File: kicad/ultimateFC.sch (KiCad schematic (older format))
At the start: 195 parts, among them J1 USB_B_Micro, J2 10132797-011100LF, J3 10132797-011100LF, J4 10132797-011100LF, J5 10132797-011100LF, J6 10132797-011100LF, Q1 DMP2066LSN-7, U1 EFM8BB21F16G-C-QFN20R, U10 NCP81253MNTBG, U11 SiZ200DT, U12 NCP81253MNTBG, U13 SiZ200DT, U14 TPS62824ADMQ, U15 SiZ200DT, U16 NCP81253MNTBG, U17 NCP81253MNTBG, U18 NCP81253MNTBG, U19 NCP81253MNTBG, U2 EFM8BB21F16G-C-QFN20R, U20 SiZ200DT, U21 SiZ200DT, U22 SiZ200DT, U23 SiZ200DT, U24 EFM8BB21F16G-C-QFN20R, U25 NCP81253MNTBG, U26 SiZ200DT, U27 NCP81253MNTBG, U28 NCP81253MNTBG, U29 SiZ200DT, U3 NCP81253MNTBG, U30 SiZ200DT, U31 INA186, U32 LMR33630CQRNX, U33 STM32F745VGHx, U34 AB7456, U35 ZOE-M8Q_ZOE-M8Q, U36 ICM-20602, U37 S25FL064L, U39 BMP280, U4 SiZ200DT, U5 TPS630701, U6 EFM8BB21F16G-C-QFN20R, U7 NCP81253MNTBG, U8 SiZ200DT, U9 NCP81253MNTBG, X1 Molex_734120110, Y1 CSTNE8M00G550000R0, Y2 ECS-270-8-47Q-CES-TR

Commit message: swap ESC gate role names, add schematic pdf
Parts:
- J1: symbol Connector:USB_B_Micro -> ultimateFC-rescue:USB_B_Micro-Connector
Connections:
- net Ac_ESC_1: now also RN14.3 (R3.1), RN14.5 (R4.2), U1.14 (P1.0), U18.2 (PWM); no longer RN14.6 (R3.2), U1.13 (P1.1)
- net Ac_ESC_2: now also RN13.3 (R3.1), RN13.5 (R4.2), U2.14 (P1.0), U3.2 (PWM); no longer RN13.6 (R3.2), U2.13 (P1.1)
- net Ac_ESC_3: now also RN15.3 (R3.1), RN15.5 (R4.2), U19.2 (PWM), U6.14 (P1.0); no longer RN15.6 (R3.2), U6.13 (P1.1)
- net Ac_ESC_4: now also RN20.3 (R3.1), RN20.5 (R4.2), U24.14 (P1.0), U28.2 (PWM); no longer RN20.6 (R3.2), U24.13 (P1.1)
- net Ap_ESC_1: now also RN14.6 (R3.2), U1.13 (P1.1); no longer RN14.3 (R3.1), RN14.5 (R4.2), U1.14 (P1.0), U18.2 (PWM)
- net Ap_ESC_2: now also RN13.6 (R3.2), U2.13 (P1.1); no longer RN13.3 (R3.1), RN13.5 (R4.2), U2.14 (P1.0), U3.2 (PWM)
- net Ap_ESC_3: now also RN15.6 (R3.2), U6.13 (P1.1); no longer RN15.3 (R3.1), RN15.5 (R4.2), U19.2 (PWM), U6.14 (P1.0)
- net Ap_ESC_4: now also RN20.6 (R3.2), U24.13 (P1.1); no longer RN20.3 (R3.1), RN20.5 (R4.2), U24.14 (P1.0), U28.2 (PWM)
- net Bc_ESC_1: now also RN14.2 (R2.1), RN14.8 (R1.2), U1.10 (P1.3), U10.2 (PWM); no longer RN14.7 (R2.2), U1.11 (P1.2)
- net Bc_ESC_2: now also RN13.2 (R2.1), RN13.8 (R1.2), U2.10 (P1.3), U7.2 (PWM); no longer RN13.7 (R2.2), U2.11 (P1.2)
- net Bc_ESC_3: now also RN15.2 (R2.1), RN15.8 (R1.2), U12.2 (PWM), U6.10 (P1.3); no longer RN15.7 (R2.2), U6.11 (P1.2)
- net Bc_ESC_4: now also RN20.2 (R2.1), RN20.8 (R1.2), U24.10 (P1.3), U25.2 (PWM); no longer RN20.7 (R2.2), U24.11 (P1.2)
- net Bp_ESC_1: now also RN14.7 (R2.2), U1.11 (P1.2); no longer RN14.2 (R2.1), RN14.8 (R1.2), U1.10 (P1.3), U10.2 (PWM)
- net Bp_ESC_2: now also RN13.7 (R2.2), U2.11 (P1.2); no longer RN13.2 (R2.1), RN13.8 (R1.2), U2.10 (P1.3), U7.2 (PWM)
- net Bp_ESC_3: now also RN15.7 (R2.2), U6.11 (P1.2); no longer RN15.2 (R2.1), RN15.8 (R1.2), U12.2 (PWM), U6.10 (P1.3)
- net Bp_ESC_4: now also RN20.7 (R2.2), U24.11 (P1.2); no longer RN20.2 (R2.1), RN20.8 (R1.2), U24.10 (P1.3), U25.2 (PWM)
- net Cc_ESC_1: now also R16.2, R17.1, U1.9 (P1.4), U16.2 (PWM); no longer R17.2, U1.8 (P1.5)
- net Cc_ESC_2: now also R26.2, R27.1, U2.9 (P1.4), U9.2 (PWM); no longer R27.2, U2.8 (P1.5)
- net Cc_ESC_3: now also R18.2, R19.1, U17.2 (PWM), U6.9 (P1.4); no longer R19.2, U6.8 (P1.5)
- net Cc_ESC_4: now also R28.2, R29.1, U24.9 (P1.4), U27.2 (PWM); no longer R29.2, U24.8 (P1.5)
- net Cp_ESC_1: now also R17.2, U1.8 (P1.5); no longer R16.2, R17.1, U1.9 (P1.4), U16.2 (PWM)
- net Cp_ESC_2: now also R27.2, U2.8 (P1.5); no longer R26.2, R27.1, U2.9 (P1.4), U9.2 (PWM)
- net Cp_ESC_3: now also R19.2, U6.8 (P1.5); no longer R18.2, R19.1, U17.2 (PWM), U6.9 (P1.4)
- net Cp_ESC_4: now also R29.2, U24.8 (P1.5); no longer R28.2, R29.1, U24.9 (P1.4), U27.2 (PWM)
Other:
- note added: "public files:\nhttps://github.com/crteensy/Yolo-files"
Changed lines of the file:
@@
 EESchema Schematic File Version 4
-LIBS:ultimateFC-cache
 EELAYER 30 0
 EELAYER END
@@
 Sheet 1 1
 Title "ESCs and Power"
-Date "2020-05-26"
-Rev "0"
+Date "2021-04-22"
+Rev "1"
 Comp ""
 Comment1 ""
@@
 Text GLabel 11050 2325 0    50   Input ~ 0
 ESC_2_TX
-Text GLabel 12450 1825 2    50   Input ~ 0
-Ap_ESC_2
 Text GLabel 12450 1925 2    50   Input ~ 0
+Ap_ESC_2
+Text GLabel 12450 1825 2    50   Input ~ 0
 Ac_ESC_2
-Text GLabel 12450 2125 2    50   Input ~ 0
-Bp_ESC_2
 Text GLabel 12450 2025 2    50   Input ~ 0
+Bp_ESC_2
+Text GLabel 12450 2125 2    50   Input ~ 0
 Bc_ESC_2
-Text GLabel 12450 2225 2    50   Input ~ 0
-Cp_ESC_2
 Text GLabel 12450 2325 2    50   Input ~ 0
+Cp_ESC_2
+Text GLabel 12450 2225 2    50   Input ~ 0
 Cc_ESC_2
 NoConn ~ 12450 2425
@@
 NoConn ~ 11050 2525
 NoConn ~ 11050 2625
-Text GLabel 15650 1875 0    50   Input ~ 0
+Text GLabel 15650 1775 0    50   Input ~ 0
 Ac_ESC_2
-Text GLabel 15675 2075 0    50   Input ~ 0
+Text GLabel 15675 1975 0    50   Input ~ 0
 Bp_ESC_2
-Text GLabel 14700 4025 0    50   Input ~ 0
-Cp_ESC_2
 Text GLabel 14700 4125 0    50   Input ~ 0
+Cp_ESC_2
+Text GLabel 14700 4025 0    50   Input ~ 0
 Cc_ESC_2
 $Comp
@@
 Wire Wire Line
 	16800 4450 16950 4450
-Text GLabel 15650 1775 0    50   Input ~ 0
+Text GLabel 15650 1875 0    50   Input ~ 0
 Ap_ESC_2
 Wire Wire Line
@@
 Text GLabel 16125 2225 3    50   Input ~ 0
 LS_2_B
-Text GLabel 15675 1975 0    50   Input ~ 0
+Text GLabel 15675 2075 0    50   Input ~ 0
 Bc_ESC_2
 $Comp
@@
 Text GLabel 1775 2325 0    50   Input ~ 0
 ESC_1_TX
-Text GLabel 3175 1825 2    50   Input ~ 0
-Ap_ESC_1
 Text GLabel 3175 1925 2    50   Input ~ 0
+Ap_ESC_1
+Text GLabel 3175 1825 2    50   Input ~ 0
 Ac_ESC_1
-Text GLabel 3175 2125 2    50   Input ~ 0
-Bp_ESC_1
 Text GLabel 3175 2025 2    50   Input ~ 0
+Bp_ESC_1
+Text GLabel 3175 2125 2    50   Input ~ 0
 Bc_ESC_1
-Text GLabel 3175 2225 2    50   Input ~ 0
-Cp_ESC_1
 Text GLabel 3175 2325 2    50   Input ~ 0
+Cp_ESC_1
+Text GLabel 3175 2225 2    50   Input ~ 0
 Cc_ESC_1
 NoConn ~ 3175 2425
@@
 NoConn ~ 1775 2525
 NoConn ~ 1775 2625
-Text GLabel 6375 1875 0    50   Input ~ 0
+Text GLabel 6375 1775 0    50   Input ~ 0
 Ac_ESC_1
-Text GLabel 6400 2075 0    50   Input ~ 0
+Text GLabel 6400 1975 0    50   Input ~ 0
 Bp_ESC_1
-Text GLabel 5425 4025 0    50   Input ~ 0
-Cp_ESC_1
 Text GLabel 5425 4125 0    50   Input ~ 0
+Cp_ESC_1
+Text GLabel 5425 4025 0    50   Input ~ 0
 Cc_ESC_1
 $Comp
@@
 Wire Wire Line
 	7525 4450 7675 4450
-Text GLabel 6375 1775 0    50   Input ~ 0
+Text GLabel 6375 1875 0    50   Input ~ 0
 Ap_ESC_1
 Wire Wire Line
@@
 Text GLabel 6850 2225 3    50   Input ~ 0
 LS_1_B
-Text GLabel 6400 1975 0    50   Input ~ 0
+Text GLabel 6400 2075 0    50   Input ~ 0
 Bc_ESC_1
 Wire Wire Line
@@
 Text GLabel 1800 7275 0    50   Input ~ 0
 ESC_3_TX
-Text GLabel 3200 6775 2    50   Input ~ 0
-Ap_ESC_3
 Text GLabel 3200 6875 2    50   Input ~ 0
+Ap_ESC_3
+Text GLabel 3200 6775 2    50   Input ~ 0
 Ac_ESC_3
-Text GLabel 3200 7075 2    50   Input ~ 0
-Bp_ESC_3
 Text GLabel 3200 6975 2    50   Input ~ 0
+Bp_ESC_3
+Text GLabel 3200 7075 2    50   Input ~ 0
 Bc_ESC_3
-Text GLabel 3200 7175 2    50   Input ~ 0
-Cp_ESC_3
 Text GLabel 3200 7275 2    50   Input ~ 0
+Cp_ESC_3
+Text GLabel 3200 7175 2    50   Input ~ 0
 Cc_ESC_3
 NoConn ~ 3200 7375
@@
 NoConn ~ 1800 7475
 NoConn ~ 1800 7575
-Text GLabel 6400 6825 0    50   Input ~ 0
+Text GLabel 6400 6725 0    50   Input ~ 0
 Ac_ESC_3
-Text GLabel 6425 7025 0    50   Input ~ 0
+Text GLabel 6425 6925 0    50   Input ~ 0
 Bp_ESC_3
-Text GLabel 5450 8975 0    50   Input ~ 0
-Cp_ESC_3
 Text GLabel 5450 9075 0    50   Input ~ 0
+Cp_ESC_3
+Text GLabel 5450 8975 0    50   Input ~ 0
 Cc_ESC_3
 $Comp
@@
 Wire Wire Line
 	7550 9400 7700 9400
-Text GLabel 6400 6725 0    50   Input ~ 0
+Text GLabel 6400 6825 0    50   Input ~ 0
 Ap_ESC_3
 Wire Wire Line
@@
 Text GLabel 6875 7175 3    50   Input ~ 0
 LS_3_B
-Text GLabel 6425 6925 0    50   Input ~ 0
+Text GLabel 6425 7025 0    50   Input ~ 0
 Bc_ESC_3
 Wire Wire Line
@@
 Text GLabel 11050 7275 0    50   Input ~ 0
 ESC_4_TX
-Text GLabel 12450 6775 2    50   Input ~ 0
-Ap_ESC_4
 Text GLabel 12450 6875 2    50   Input ~ 0
+Ap_ESC_4
+Text GLabel 12450 6775 2    50   Input ~ 0
 Ac_ESC_4
-Text GLabel 12450 7075 2    50   Input ~ 0
-Bp_ESC_4
 Text GLabel 12450 6975 2    50   Input ~ 0
+Bp_ESC_4
+Text GLabel 12450 7075 2    50   Input ~ 0
 Bc_ESC_4
-Text GLabel 12450 7175 2    50   Input ~ 0
-Cp_ESC_4
 Text GLabel 12450 7275 2    50   Input ~ 0
+Cp_ESC_4
+Text GLabel 12450 7175 2    50   Input ~ 0
 Cc_ESC_4
 NoConn ~ 12450 7375
@@
 NoConn ~ 11050 7475
 NoConn ~ 11050 7575
-Text GLabel 15650 6825 0    50   Input ~ 0
+Text GLabel 15650 6725 0    50   Input ~ 0
 Ac_ESC_4
-Text GLabel 15675 7025 0    50   Input ~ 0
+Text GLabel 15675 6925 0    50   Input ~ 0
 Bp_ESC_4
-Text GLabel 14700 8975 0    50   Input ~ 0
-Cp_ESC_4
 Text GLabel 14700 9075 0    50   Input ~ 0
+Cp_ESC_4
+Text GLabel 14700 8975 0    50   Input ~ 0
 Cc_ESC_4
 $Comp
@@
 Wire Wire Line
 	16800 9400 16950 9400
-Text GLabel 15650 6725 0    50   Input ~ 0
+Text GLabel 15650 6825 0    50   Input ~ 0
 Ap_ESC_4
 Wire Wire Line
@@
 Text GLabel 16125 7175 3    50   Input ~ 0
 LS_4_B
-Text GLabel 15675 6925 0    50   Input ~ 0
+Text GLabel 15675 7025 0    50   Input ~ 0
 Bc_ESC_4
 Wire Wire Line
@@
 	25750 1175 25850 1175
 $Comp
-L Connector:USB_B_Micro J?
+L ultimateFC-rescue:USB_B_Micro-Connector J?
 U 1 1 5F57339B
 P 27000 2425
@@
 Wire Wire Line
 	10300 14775 10000 14775
+Text Notes 26325 10600 0    150  ~ 0
+public files:\nhttps://github.com/crteensy/Yolo-files
 $EndSCHEMATC

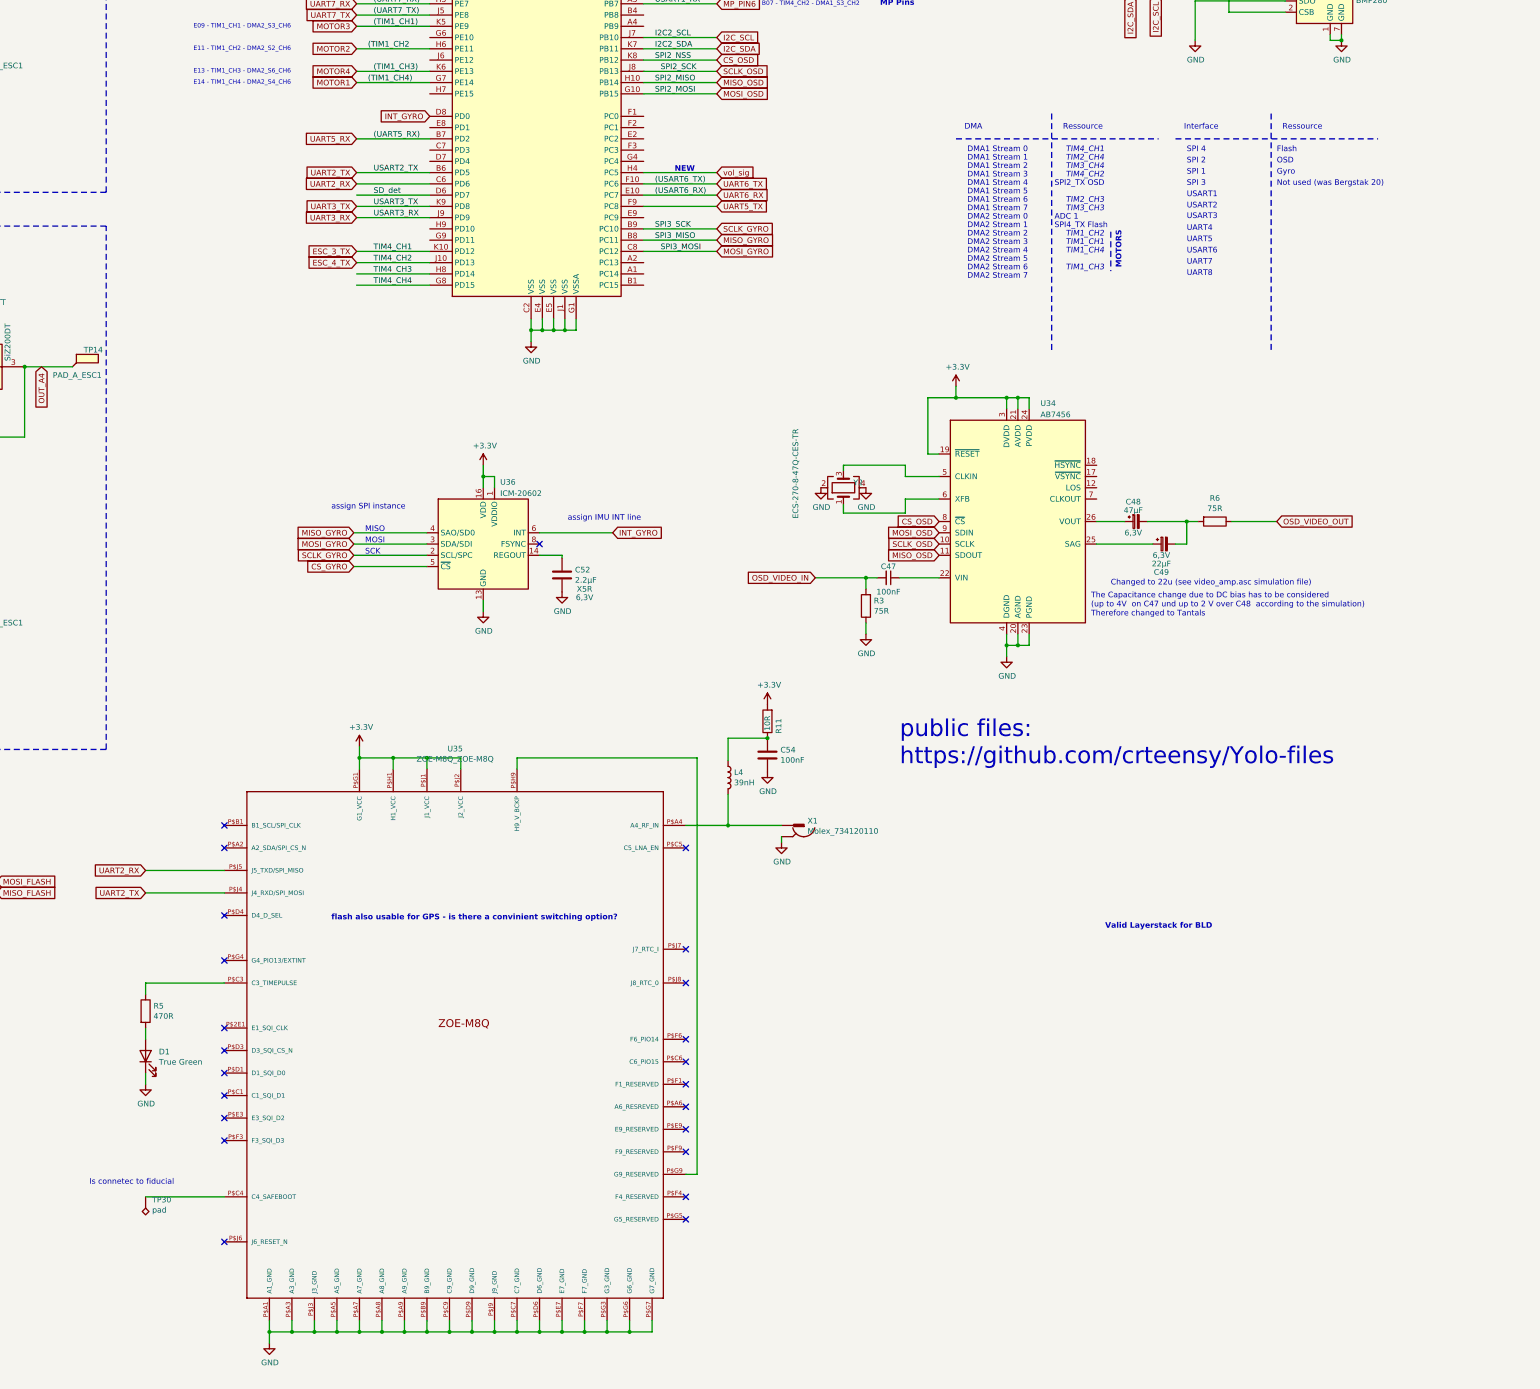
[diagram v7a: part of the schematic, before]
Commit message: add license info to schematic, add schematic pdf
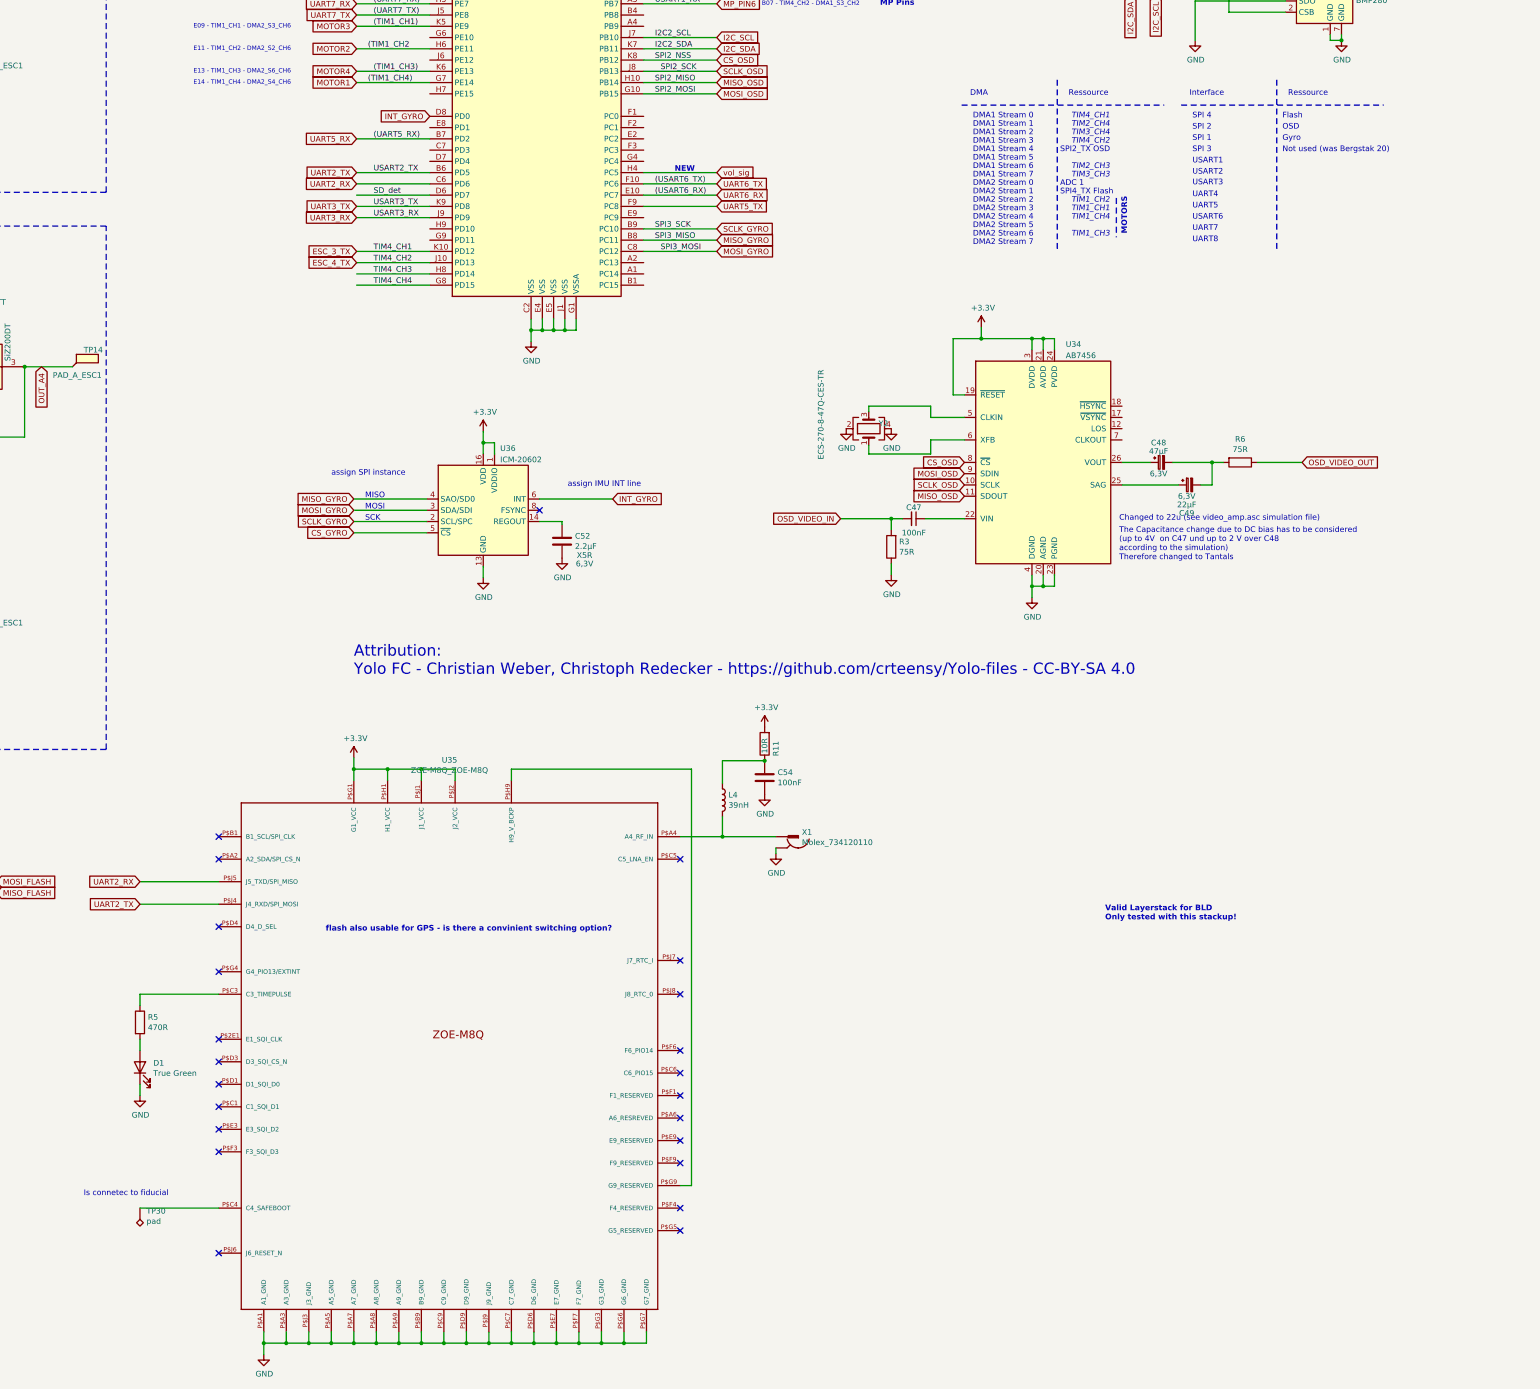
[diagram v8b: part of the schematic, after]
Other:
- note added: "Attribution:\nYolo FC - Christian Weber, Christoph Redecker - https://github.com/crteensy/Yolo-files - CC-BY-SA 4.0"
- note added: "The Capacitance change due to DC bias has to be considered \n(up to 4V on C47 und up to 2 V over C48 \naccording to the simulation)\nTherefore changed to Tantals"
- note added: "Valid Layerstack for BLD\nOnly tested with this stackup!"
- note removed: "The Capacitance change due to DC bias has to be considered \n(up to 4V on C47 und up to 2 V over C48 according to the simulation)\nTherefore changed to Tantals"
- note removed: "Valid Layerstack for BLD"
- note removed: "public files:\nhttps://github.com/crteensy/Yolo-files"
- moved on the sheet: C47, C48, C49, C52, C54, D1, L4, R11, R3, R5, R6, TP30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
